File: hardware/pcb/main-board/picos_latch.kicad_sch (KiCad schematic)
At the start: 6 parts, among them Q1105 DMG2302U, Q1106 DMG2301L

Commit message: make a start on RP2040 to replace the KB pico
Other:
- title: Z88R - Z88 Recreated -> Z88R - Z88 Recreation
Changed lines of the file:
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@@
 	(paper "A4")
 	(title_block
-		(title "Z88R - Z88 Recreated")
-		(date "2025-12-19")
-		(rev "20251219WIP")
+		(title "Z88R - Z88 Recreation")
+		(date "2025-12-30")
+		(rev "20251230WIP")
 		(company "Fountain and Menadue")
 	)

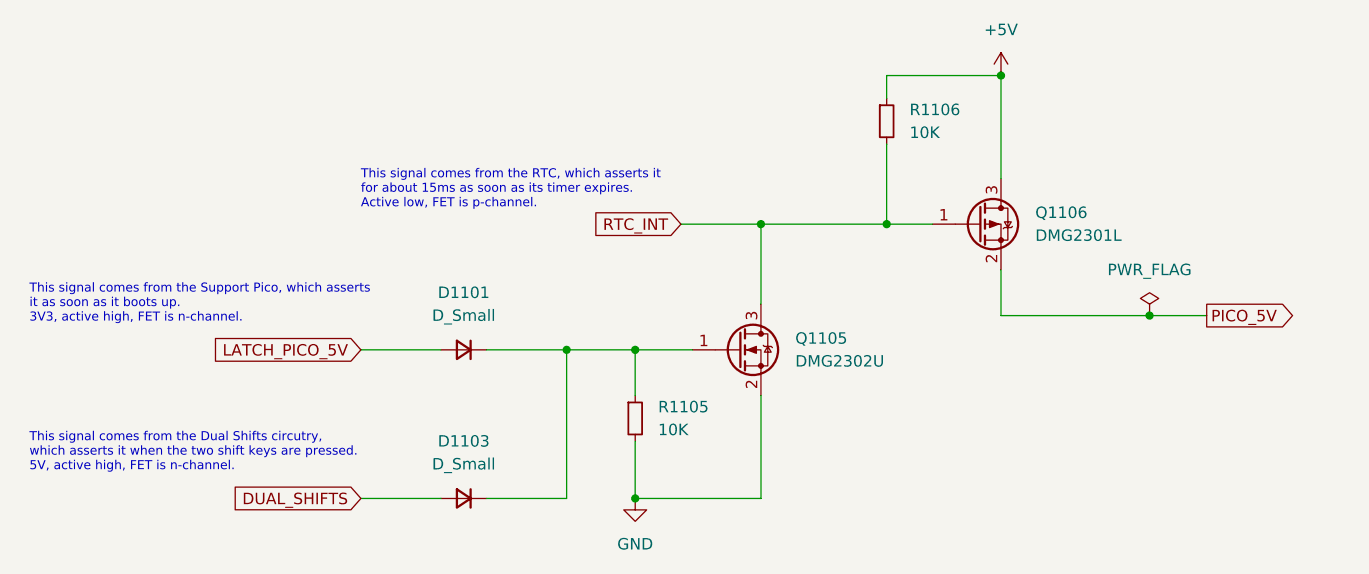
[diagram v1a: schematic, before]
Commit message: start the support pico rp2040 replacement
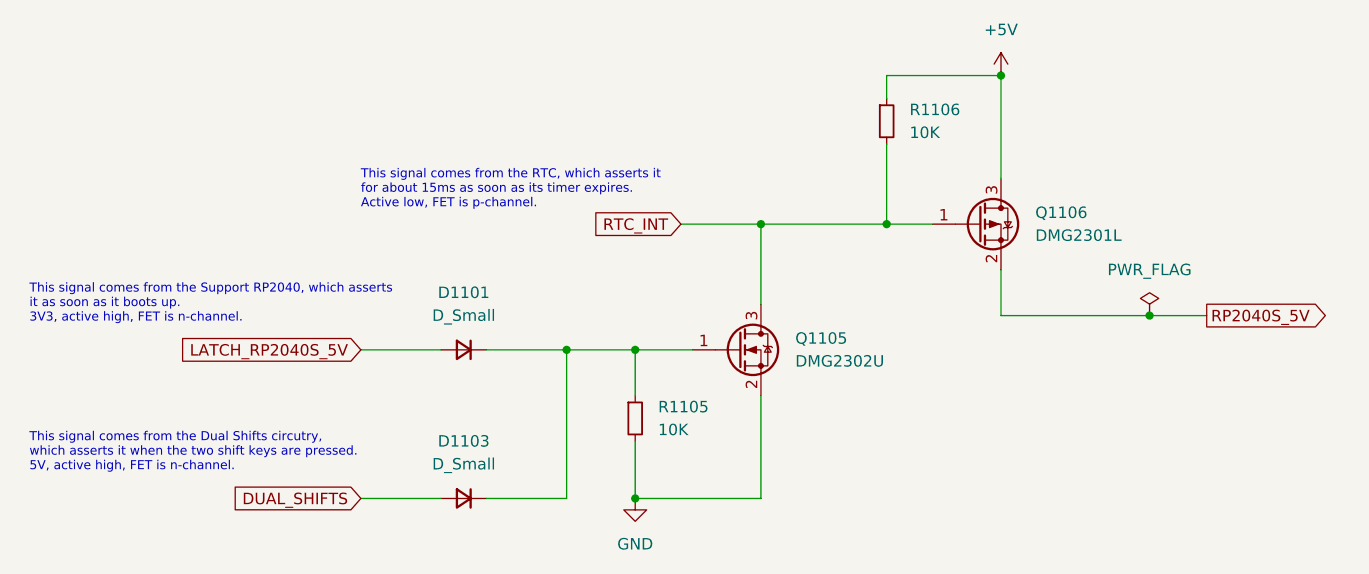
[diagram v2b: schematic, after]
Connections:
- net LATCH_PICO_5V renamed LATCH_RP2040S_5V
- net PICO_5V renamed RP2040S_5V
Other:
- note added: "This signal comes from the Support RP2040, which asserts it as soon as it boots up. 3V3, active high, FET is n-channel."
- note removed: "This signal comes from the Support Pico, which asserts it as soon as it boots up. 3V3, active high, FET is n-channel."
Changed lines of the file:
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@@
 	(title_block
 		(title "Z88R - Z88 Recreation")
-		(date "2025-12-30")
-		(rev "20251230WIP")
+		(date "2026-01-01")
+		(rev "20260101WIP")
 		(company "Fountain and Menadue")
 	)
@@
 		)
 	)
-	(text "This signal comes from the Support Pico, which asserts\nit as soon as it boots up.\n3V3, active high, FET is n-channel."
+	(text "This signal comes from the Support RP2040, which asserts\nit as soon as it boots up.\n3V3, active high, FET is n-channel."
 		(exclude_from_sim no)
 		(at 20.32 52.07 0)
@@
 		)
 	)
-	(global_label "LATCH_PICO_5V"
+	(global_label "LATCH_RP2040S_5V"
 		(shape input)
 		(at 57.15 57.15 180)
@@
 		)
 		(property "Intersheetrefs" "${INTERSHEET_REFS}"
-			(at 40.4256 57.15 0)
+			(at 36.3134 57.15 0)
 			(effects
 				(font
@@
 		)
 	)
-	(global_label "PICO_5V"
+	(global_label "RP2040S_5V"
 		(shape output)
 		(at 151.13 53.34 0)
@@
 		)
 		(property "Intersheetrefs" "${INTERSHEET_REFS}"
-			(at 161.202 53.34 0)
+			(at 165.3142 53.34 0)
 			(effects
 				(font

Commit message: a few more tidyups, almost ready for dual shifts stuff now
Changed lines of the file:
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@@
 	(text "This signal comes from the Support RP2040, which asserts\nit as soon as it boots up.\n3V3, active high, FET is n-channel."
 		(exclude_from_sim no)
-		(at 20.32 52.07 0)
+		(at 19.05 50.8 0)
 		(effects
 			(font
